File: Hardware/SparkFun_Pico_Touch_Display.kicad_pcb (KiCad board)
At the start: 4 copper layers, 58.4 x 50.8 mm, 89 parts, among them J1 Conn_01x20, J2 Conn_01x20, J3 Conn_02x10_SMD_RA, J4 Conn_1x21_FPC, J5 Qwiic_Vertical, J6 microSD, Q1 RE1C002UNTCL, SW1 SMD_4.6x2.8mm_h2.5mm, U1 2" LCD-TFT 240x320, U2 PCA9554PW

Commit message: Change GPIO expander to PCA9534
PCA9554 has internal pull-up resistors on IO pins, whereas PCA9534 does not. The pull-up resistors were causing problems with the camera not being enabled by default, so this will ensure the camera's pull-up/down resistors take priority.
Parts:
- U2: value PCA9554PW -> PCA9534PW
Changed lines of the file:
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@@
 		(tags "SparkFun")
 		(property "Reference" "Q1"
-			(at 0 0.9 360)
+			(at 0 0.9 0)
 			(layer "B.Fab")
 			(effects
@@
 		)
 		(property "Value" "RE1C002UNTCL"
-			(at 0 -2 360)
+			(at 0 -2 0)
 			(layer "B.Fab")
 			(effects
@@
 			)
 		)
-		(property "Value" "PCA9554PW"
+		(property "Value" "PCA9534PW"
 			(at 0 -3.45 0)
 			(layer "B.Fab")
@@
 			)
 		)
-		(property "Datasheet" "https://www.ti.com/lit/ds/symlink/tca9554.pdf"
+		(property "Datasheet" "https://www.ti.com/lit/ds/symlink/tca9534.pdf"
 			(at 0 0 180)
 			(unlocked yes)
@@
 			)
 		)
-		(property "PROD_ID" "IC-23589"
+		(property "PROD_ID" "IC-26490"
 			(at 0 0 180)
 			(unlocked yes)

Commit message: Bump version number to v10
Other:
- board text added: "v10"
- board text removed: "v01"
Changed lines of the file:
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@@
 	(title_block
 		(title "SparkFun Pico Touch Display")
-		(date "2025-02-27")
-		(rev "v01")
+		(date "2025-05-07")
+		(rev "v10")
 		(company "SparkFun Electronics")
 		(comment 1 "Designed by: Dryw Wade")
@@
 		(layer "Edge.Cuts")
 	)
-	(gr_text "v01"
+	(gr_text "v10"
 		(at 131.445 123.19 0)
 		(layer "B.Cu" knockout)

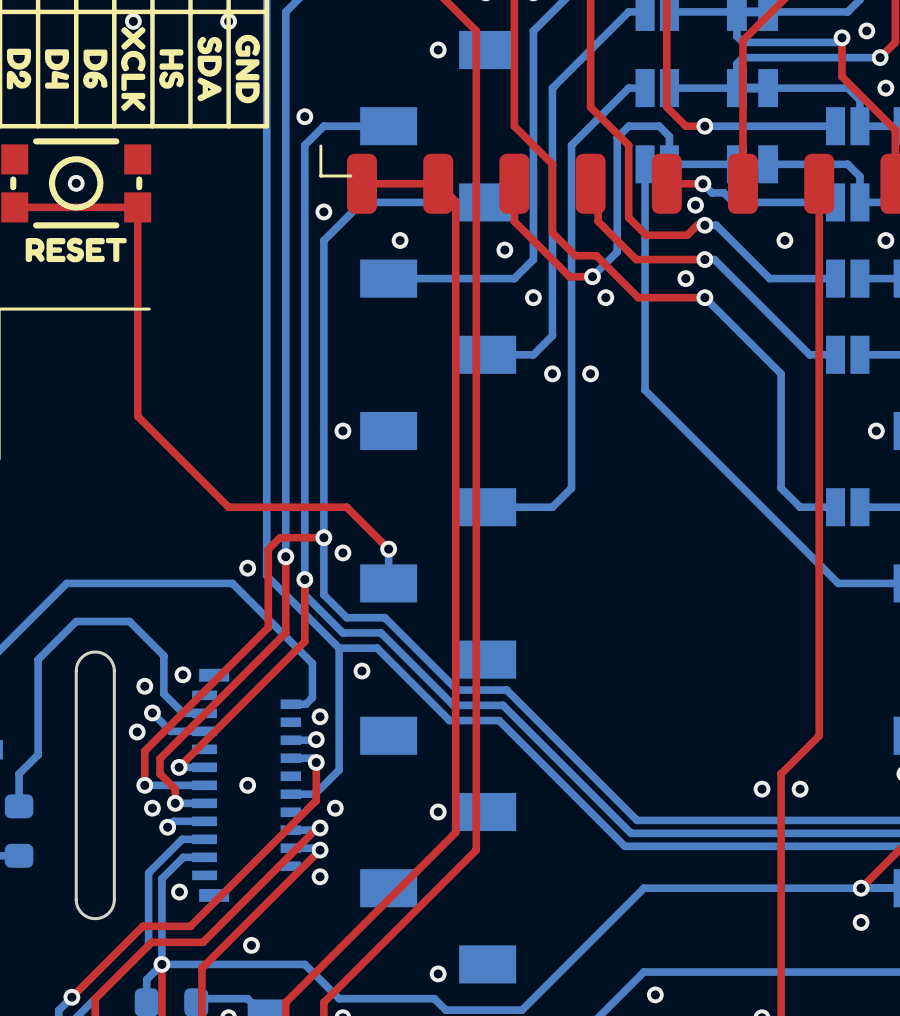
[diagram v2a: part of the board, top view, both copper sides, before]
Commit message: Fix acid trap on PWDN pad
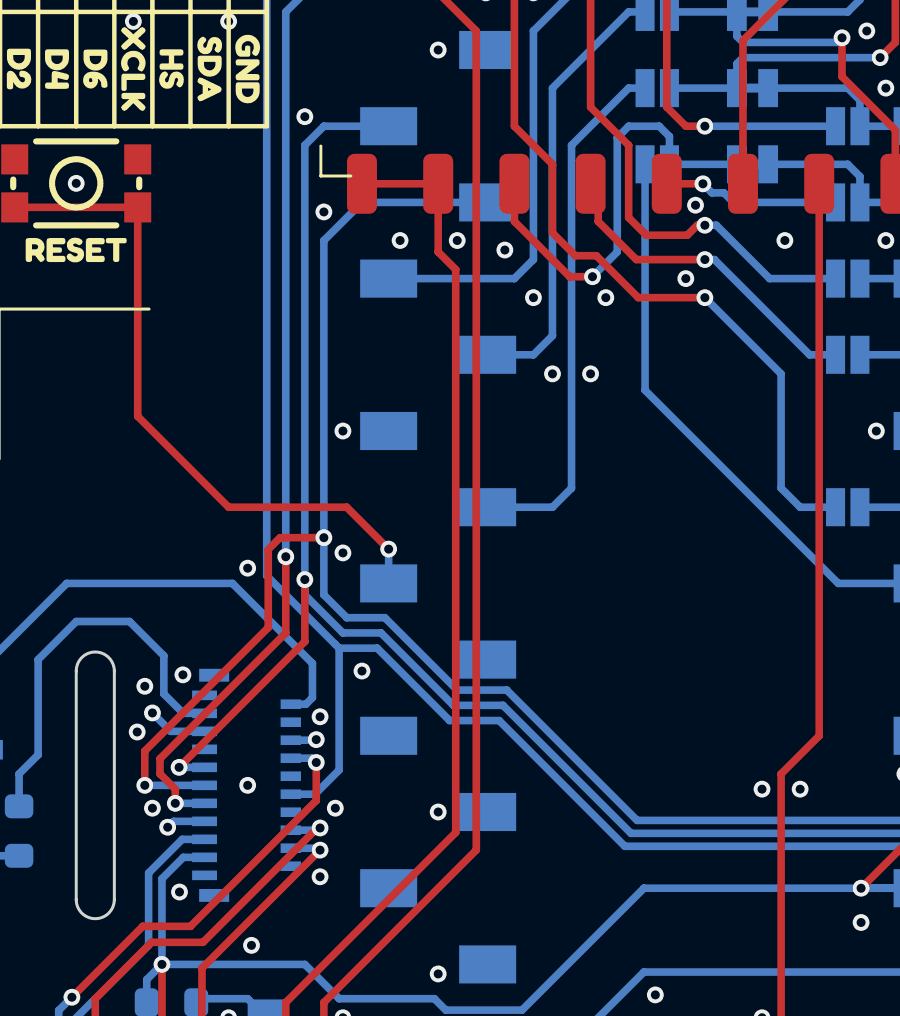
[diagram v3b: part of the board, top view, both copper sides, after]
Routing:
- net GND: vias 96 -> 97
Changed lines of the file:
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@@
+	)
+	(via
+		(at 136.525 86.36)
+		(size 0.56)
+		(drill 0.3)
+		(layers "F.Cu" "B.Cu")
+		(free yes)
+		(net 3)
 	)
 	(via
@@
 	)
 	(segment
+		(start 136.4748 87.3258)
+		(end 135.89 86.741)
+		(width 0.254)
+		(layer "F.Cu")
+		(net 20)
+	)
+	(segment
+		(start 129.794 116.586)
+		(end 130.81 115.57)
+		(width 0.254)
+		(layer "F.Cu")
+		(net 20)
+	)
+	(segment
 		(start 136.4748 106.0952)
-		(end 136.4748 85.0548)
+		(end 136.4748 87.3258)
+		(width 0.254)
+		(layer "F.Cu")
+		(net 20)
+	)
+	(segment
+		(start 130.81 115.57)
+		(end 130.81 111.76)
 		(width 0.254)
 		(layer "F.Cu")
@@
 	)
 	(segment
-		(start 136.4748 85.0548)
+		(start 135.89 86.741)
 		(end 135.89 84.47)
 		(width 0.254)
 		(layer "F.Cu")
-		(net 20)
-	)
-	(segment
-		(start 129.794 116.586)
-		(end 130.81 115.57)
-		(width 0.254)
-		(layer "F.Cu")
-		(net 20)
-	)
-	(segment
-		(start 130.81 115.57)
-		(end 130.81 111.76)
-		(width 0.254)
-		(layer "F.Cu")

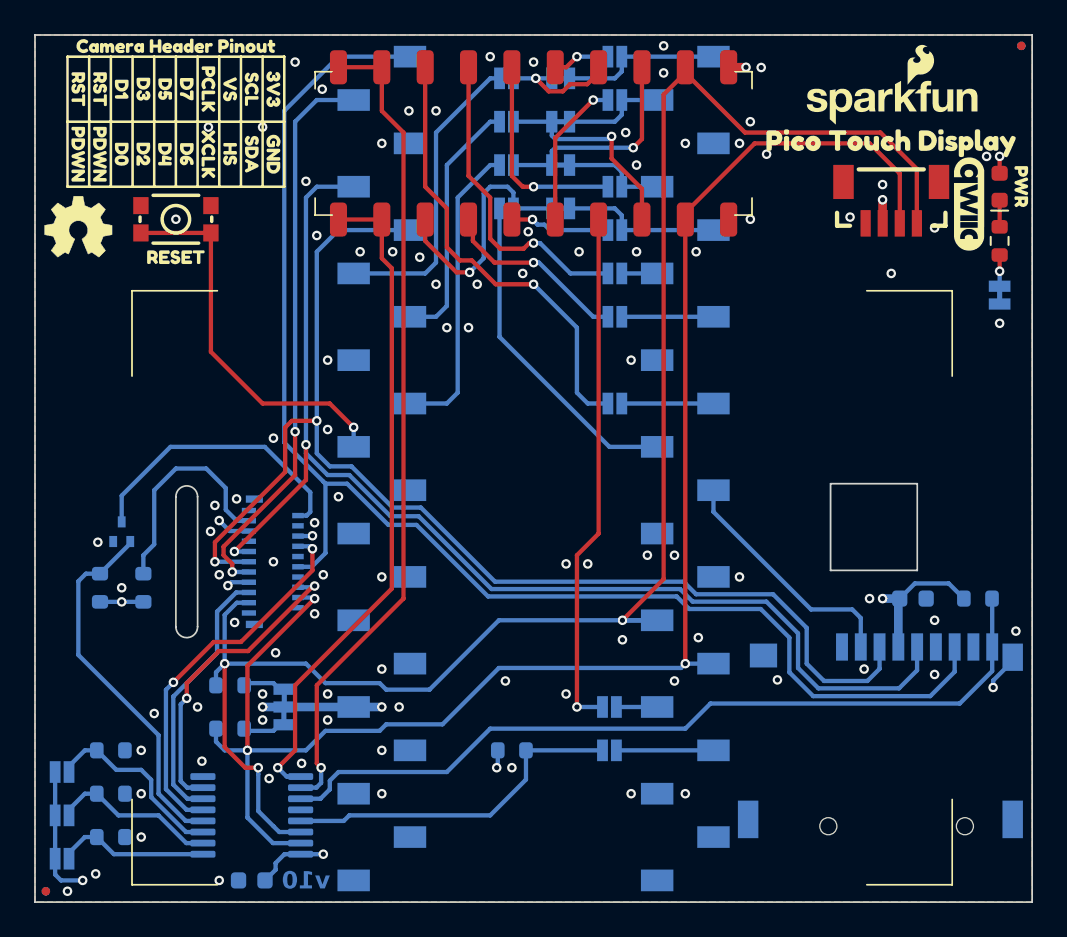
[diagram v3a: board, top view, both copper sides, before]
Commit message: Add silk about 2x9 camera header position
Also nudge header down to accommodate
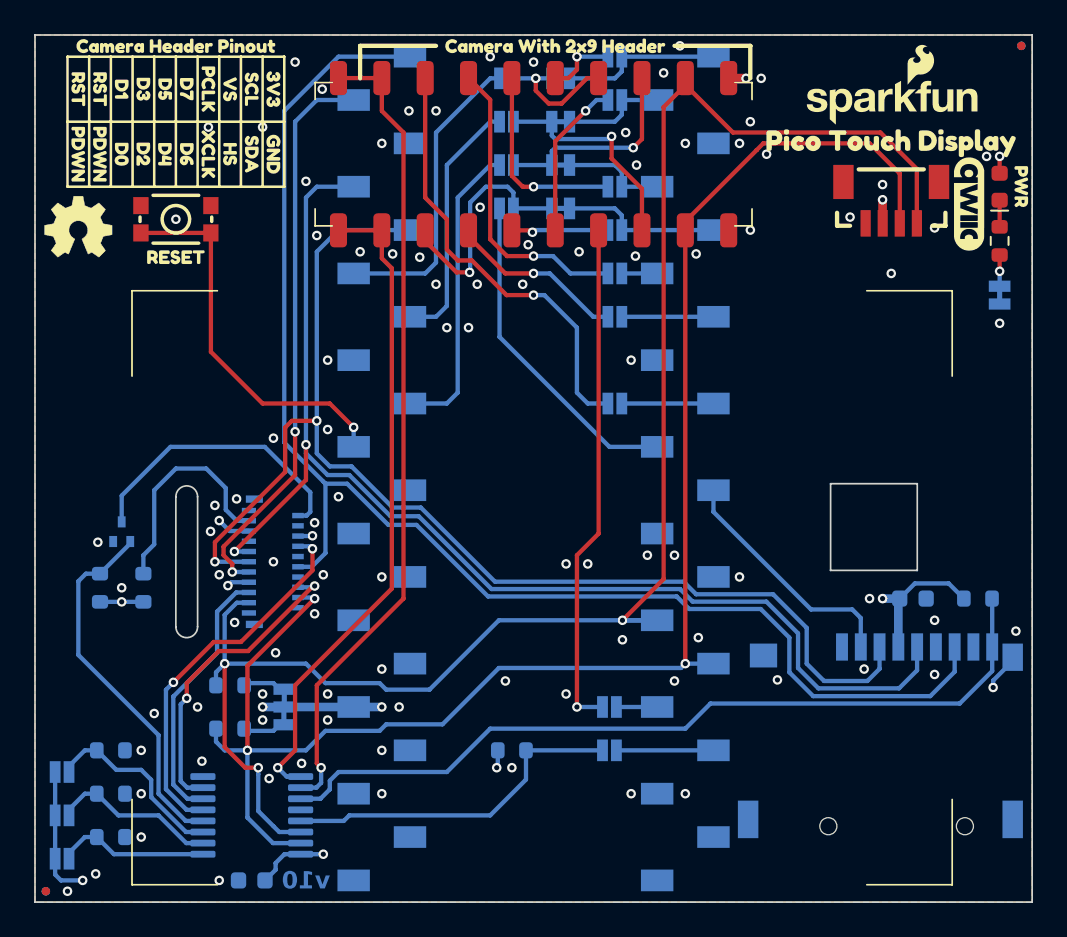
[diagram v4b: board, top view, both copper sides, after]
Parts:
- added kibuzzard-681E525B: G***, kibuzzard-681E525B, F.Cu at (146.1, 74.3)
- moved J3 0.63 mm to (144.8, 80.6)
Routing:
- net CAM_D3: track 18.6 -> 17.7 mm
- net CAM_D7: track 3.34 -> 4.05 mm
- net CAM_~{RST}: track 48.5 -> 47.9 mm
- net CAM_VS: track 12.8 -> 12.2 mm
- net CAM_PWDN: track 39.2 -> 38.6 mm
- net CAM_MCLK: track 30.6 -> 29.9 mm
- net CAM_HS: track 12.3 -> 13.0 mm
- net CAM_D5: track 12.3 -> 11.6 mm
- net CAM_D2: track 11.1 -> 10.5 mm
- net CAM_D1: track 26.5 -> 26.0 mm
- net CAM_PCLK: track 7.02 -> 7.58 mm
- net CAM_D6: track 8.78 -> 9.31 mm
- net GND: vias 97 -> 98

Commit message: Rename MCLK to XCLK
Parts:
- removed kibuzzard-67B3FFA5: G***, kibuzzard-67B3FFA5
- added kibuzzard-681E5A39: G***, kibuzzard-681E5A39, B.Cu at (146.2, 113.0)
- JP13: value MCLK -> XCLK
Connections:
- net CAM_MCLK renamed CAM_XCLK

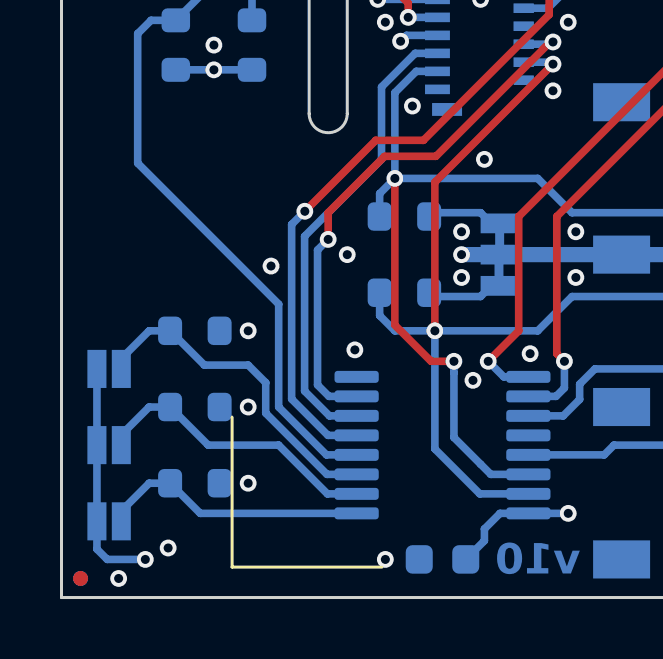
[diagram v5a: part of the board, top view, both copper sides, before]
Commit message: Add pullup resistors to TP and DISP RST nets
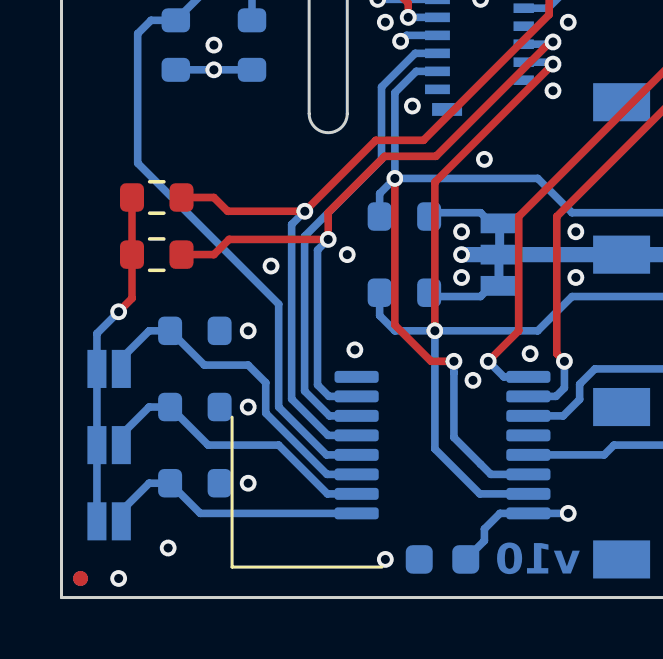
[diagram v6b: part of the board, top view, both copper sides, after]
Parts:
- added R11: 100k, SparkFun-Resistor:R_0603_1608Metric, F.Cu at (118.7, 113.0)
- added R12: 100k, SparkFun-Resistor:R_0603_1608Metric, F.Cu at (118.7, 111.1)
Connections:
- net CAM_~{RST} renamed CAM_RST
- net TP_~{RESET} renamed TP_~{RST}
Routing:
- net TP_~{RST}: track 18.2 -> 23.3 mm
- net DISP_~{RST}: track 22.1 -> 26.4 mm
- net 3.3V: track 37.9 -> 41.5 mm
